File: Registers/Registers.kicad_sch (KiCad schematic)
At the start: 27 parts, among them J1 Conn_01x08_Socket, J2 Conn_01x08_Socket, J3 Conn_01x06_Pin, U1 SN74HCT245N, U2 74LS173, U3 74LS173

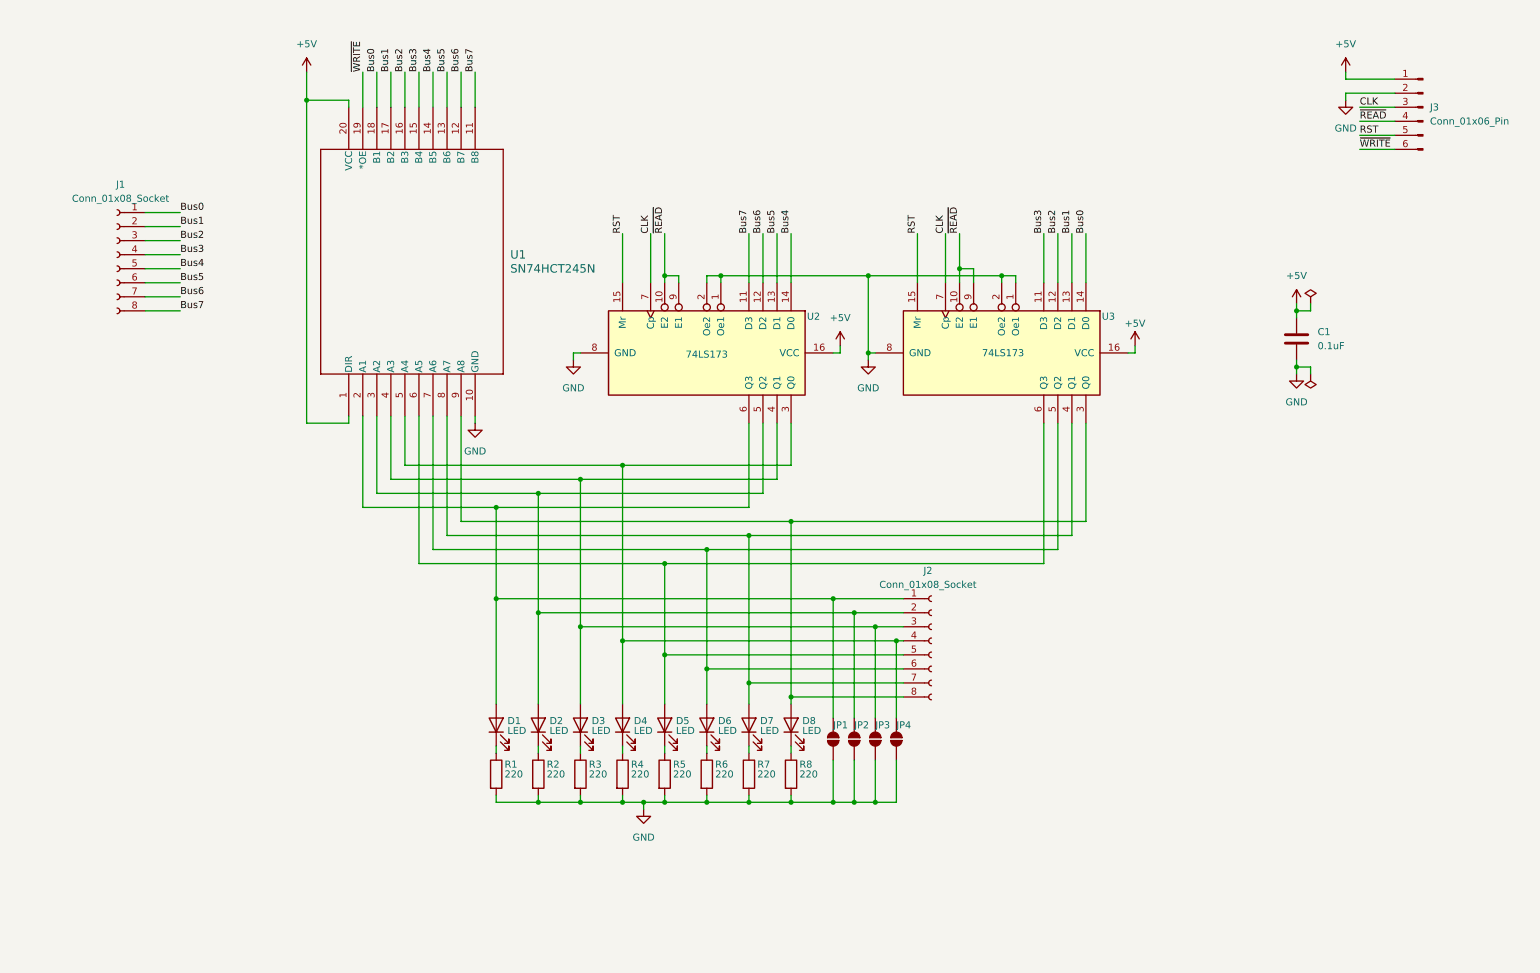
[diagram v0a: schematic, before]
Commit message: Finished routing for registers. Silkscreen and PCB shape needs to be finalized.
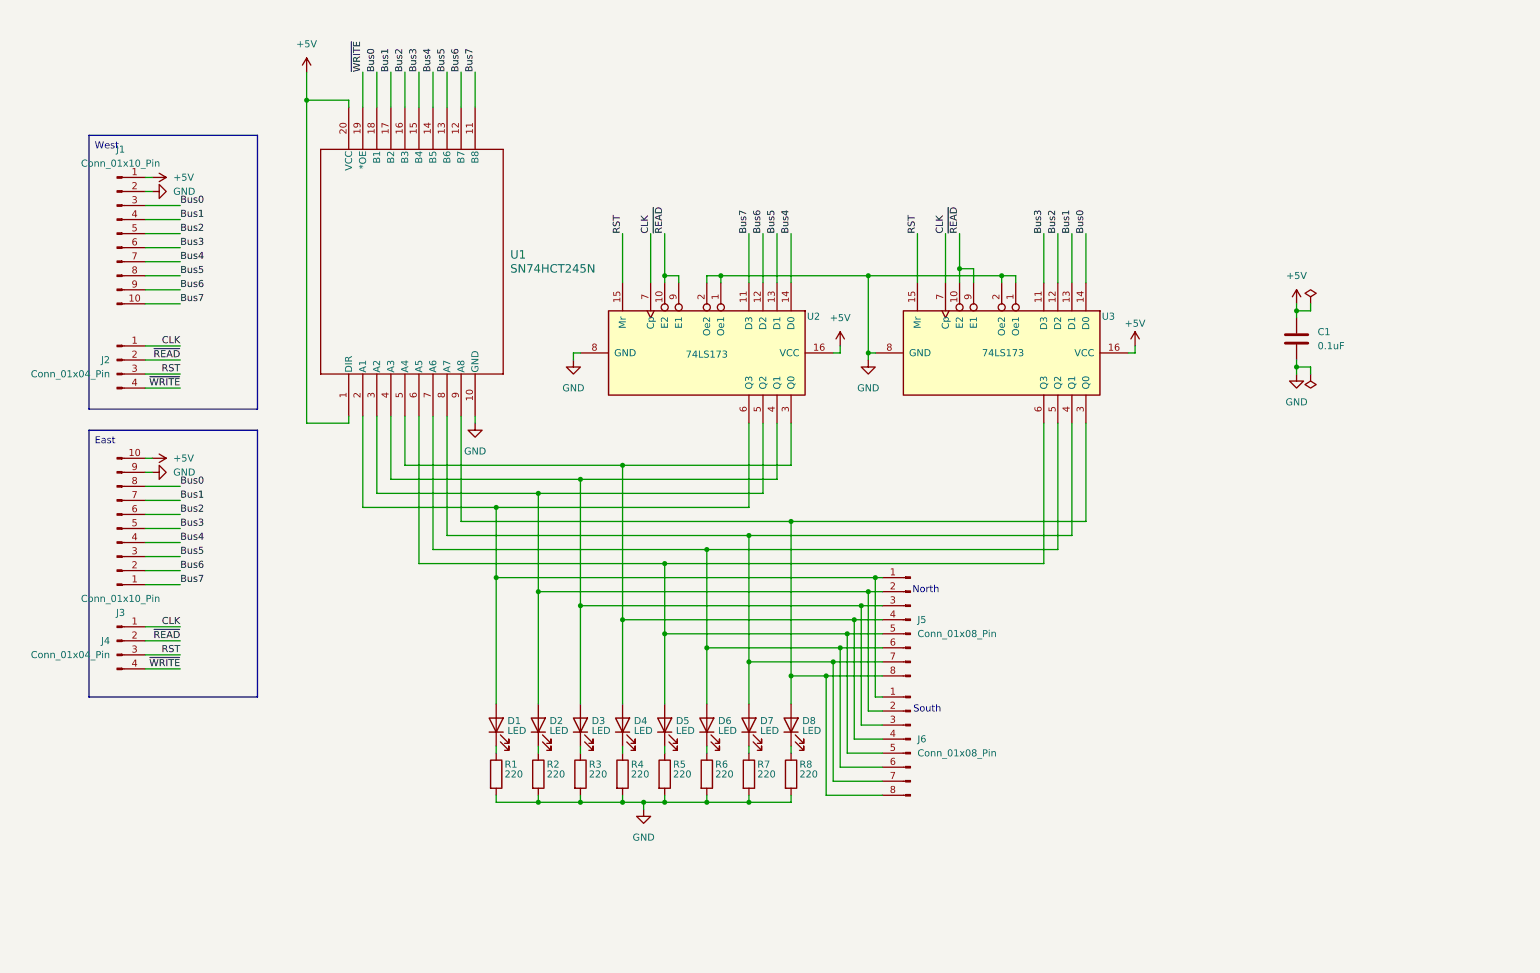
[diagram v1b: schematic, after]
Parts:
- removed J1, J2: Conn_01x08_Socket, Connector_PinHeader_1.00mm:PinHeader_1x08_P1.00mm_Horizontal, symbol Connector:Conn_01x08_Socket
- removed J3: Conn_01x06_Pin, Connector_PinHeader_1.00mm:PinHeader_1x06_P1.00mm_Horizontal, symbol Connector:Conn_01x06_Pin
- removed JP1, JP2, JP3, JP4: SolderJumper_2_Open, Jumper:SolderJumper-2_P1.3mm_Open_RoundedPad1.0x1.5mm, symbol Jumper:SolderJumper_2_Open
- added J1, J3: Conn_01x10_Pin, Connector_PinHeader_2.54mm:PinHeader_1x10_P2.54mm_Vertical, symbol Connector:Conn_01x10_Pin
- added J2, J4: Conn_01x04_Pin, Connector_PinHeader_2.54mm:PinHeader_1x04_P2.54mm_Vertical, symbol Connector:Conn_01x04_Pin
- added J5, J6: Conn_01x08_Pin, Connector_PinHeader_2.54mm:PinHeader_1x08_P2.54mm_Vertical, symbol Connector:Conn_01x08_Pin
- D1, D2, D3, D4, D5, D6, D7, D8: footprint LED_THT:LED_D2.0mm_W4.8mm_H2.5mm_FlatTop -> LED_THT:LED_D5.0mm
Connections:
- net +5V: now also J1.1 (Pin_1), J3.10 (Pin_10)
- net Bus0: now also J1.3 (Pin_3), J3.8 (Pin_8)
- net Bus1: now also J1.4 (Pin_4), J3.7 (Pin_7)
- net Bus2: now also J1.5 (Pin_5), J3.6 (Pin_6)
- net Bus3: now also J1.6 (Pin_6), J3.5 (Pin_5)
- net Bus4: now also J1.7 (Pin_7), J3.4 (Pin_4)
- net Bus5: now also J1.8 (Pin_8), J3.3 (Pin_3)
- net Bus6: now also J1.9 (Pin_9), J3.2 (Pin_2)
- net Bus7: now also J1.10 (Pin_10), J3.1 (Pin_1)
- net CLK: now also J2.1 (Pin_1), J4.1 (Pin_1)
- net GND: now also J1.2 (Pin_2), J3.9 (Pin_9)
- net RST: now also J2.3 (Pin_3), J4.3 (Pin_3)
- net ~{READ}: now also J2.2 (Pin_2), J4.2 (Pin_2)
- net ~{WRITE}: now also J2.4 (Pin_4), J4.4 (Pin_4)
- net at D8.2 (A), U1.9 (A8), U3.3 (Q0): now also J5.8 (Pin_8), J6.8 (Pin_8)
- net at D1.2 (A), U1.2 (A1), U2.6 (Q3): now also J5.1 (Pin_1), J6.1 (Pin_1)
- net at D2.2 (A), U1.3 (A2), U2.5 (Q2): now also J5.2 (Pin_2), J6.2 (Pin_2)
- net at D3.2 (A), U1.4 (A3), U2.4 (Q1): now also J5.3 (Pin_3), J6.3 (Pin_3)
- net at D4.2 (A), U1.5 (A4), U2.3 (Q0): now also J5.4 (Pin_4), J6.4 (Pin_4)
- net at D5.2 (A), U1.6 (A5), U3.6 (Q3): now also J5.5 (Pin_5), J6.5 (Pin_5)
- net at D6.2 (A), U1.7 (A6), U3.5 (Q2): now also J5.6 (Pin_6), J6.6 (Pin_6)
- net at D7.2 (A), U1.8 (A7), U3.4 (Q1): now also J5.7 (Pin_7), J6.7 (Pin_7)
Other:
- note added: "North"
- note added: "South"

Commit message: Register layout complete.
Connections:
- net Bus0: now also U2.11 (D3); no longer U3.14 (D0)
- net Bus1: now also U2.12 (D2); no longer U3.13 (D1)
- net Bus2: now also U2.13 (D1); no longer U3.12 (D2)
- net Bus3: now also U2.14 (D0); no longer U3.11 (D3)
- net Bus4: now also U3.11 (D3); no longer U2.14 (D0)
- net Bus5: now also U3.12 (D2); no longer U2.13 (D1)
- net Bus6: now also U3.13 (D1); no longer U2.12 (D2)
- net Bus7: now also U3.14 (D0); no longer U2.11 (D3)
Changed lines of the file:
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@@
 	)
 	(label "Bus7"
-		(at 142.24 62.23 90)
+		(at 203.2 62.23 90)
 		(fields_autoplaced yes)
 		(effects
@@
 	)
 	(label "Bus5"
-		(at 147.32 62.23 90)
+		(at 198.12 62.23 90)
 		(fields_autoplaced yes)
 		(effects
@@
 	)
 	(label "Bus3"
-		(at 195.58 62.23 90)
+		(at 149.86 62.23 90)
 		(fields_autoplaced yes)
 		(effects
@@
 	)
 	(label "Bus1"
-		(at 200.66 62.23 90)
+		(at 144.78 62.23 90)
 		(fields_autoplaced yes)
 		(effects
@@
 	)
 	(label "Bus4"
-		(at 149.86 62.23 90)
+		(at 195.58 62.23 90)
 		(fields_autoplaced yes)
 		(effects
@@
 	)
 	(label "Bus2"
-		(at 198.12 62.23 90)
+		(at 147.32 62.23 90)
 		(fields_autoplaced yes)
 		(effects
@@
 	)
 	(label "Bus6"
-		(at 144.78 62.23 90)
+		(at 200.66 62.23 90)
 		(fields_autoplaced yes)
 		(effects
@@
 	)
 	(label "Bus0"
-		(at 203.2 62.23 90)
-		(fields_autoplaced yes)
-		(effects
+		(at 142.24 62.23 90)
+		(fields_autoplaced yes)
+		(effects

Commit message: Added pulling resistors to unused pins from bus. (Output 2s comp & B reg write out)
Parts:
- added R9: 10k, _DownloadFootprints:CF_series_Resistors_THT, symbol Device:R
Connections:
- net +5V: now also R9.1
- net ~{WRITE}: now also R9.2
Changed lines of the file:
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@@
 		)
 	)
-	(label "Bus4"
-		(at 195.58 62.23 90)
+	(label "~{WRITE}"
+		(at 48.26 182.88 270)
 		(fields_autoplaced yes)
 		(effects
@@
 				(size 1.27 1.27)
 			)
-			(justify left bottom)
-		)
-	)
-	(label "~{READ}"
-		(at 39.37 135.89 180)
+			(justify right bottom)
+		)
+	)
+	(label "Bus4"
+		(at 195.58 62.23 90)
 		(fields_autoplaced yes)
 		(effects
@@
 				(size 1.27 1.27)
 			)
-			(justify right bottom)
-		)
-	)
-	(label "Bus4"
-		(at 39.37 118.11 0)
+			(justify left bottom)
+		)
+	)
+	(label "~{READ}"
+		(at 39.37 135.89 180)
 		(fields_autoplaced yes)
 		(effects
@@
 				(size 1.27 1.27)
 			)
-			(justify left bottom)
-		)
-	)
-	(label "Bus3"
-		(at 39.37 64.77 0)
+			(justify right bottom)
+		)
+	)
+	(label "Bus4"
+		(at 39.37 118.11 0)
 		(fields_autoplaced yes)
 		(effects
@@
 		)
 	)
-	(label "Bus2"
-		(at 39.37 62.23 0)
+	(label "Bus3"
+		(at 39.37 64.77 0)
 		(fields_autoplaced yes)
 		(effects
@@
 	)
 	(label "Bus2"
-		(at 147.32 62.23 90)
+		(at 39.37 62.23 0)
 		(fields_autoplaced yes)
 		(effects
@@
 		)
 	)
-	(label "Bus5"
-		(at 39.37 69.85 0)
+	(label "Bus2"
+		(at 147.32 62.23 90)
 		(fields_autoplaced yes)
 		(effects
@@
 		)
 	)
-	(label "Bus0"
-		(at 39.37 107.95 0)
+	(label "Bus5"
+		(at 39.37 69.85 0)
 		(fields_autoplaced yes)
 		(effects
@@
 		)
 	)
-	(label "Bus5"
-		(at 39.37 120.65 0)
+	(label "Bus0"
+		(at 39.37 107.95 0)
 		(fields_autoplaced yes)
 		(effects
@@
 		)
 	)
-	(label "~{WRITE}"
-		(at 39.37 90.17 180)
+	(label "Bus5"
+		(at 39.37 120.65 0)
 		(fields_autoplaced yes)
 		(effects
@@
 				(size 1.27 1.27)
 			)
-			(justify right bottom)
-		)
-	)
-	(label "Bus1"
-		(at 77.47 33.02 90)
+			(justify left bottom)
+		)
+	)
+	(label "~{WRITE}"
+		(at 39.37 90.17 180)
 		(fields_autoplaced yes)
 		(effects
@@
 				(size 1.27 1.27)
 			)
-			(justify left bottom)
-		)
-	)
-	(label "CLK"
-		(at 124.46 62.23 90)
+			(justify right bottom)
+		)
+	)
+	(label "Bus1"
+		(at 77.47 33.02 90)
 		(fields_autoplaced yes)
 		(effects
@@
 	)
 	(label "CLK"
-		(at 177.8 62.23 90)
+		(at 124.46 62.23 90)
 		(fields_autoplaced yes)
 		(effects
@@
 		)
 	)
-	(label "Bus6"
-		(at 90.17 33.02 90)
+	(label "CLK"
+		(at 177.8 62.23 90)
 		(fields_autoplaced yes)
 		(effects
@@
 		)
 	)
-	(label "CLK"
-		(at 39.37 82.55 180)
+	(label "Bus6"
+		(at 90.17 33.02 90)
 		(fields_autoplaced yes)
 		(effects
@@
 				(size 1.27 1.27)
 			)
-			(justify right bottom)
-		)
-	)
-	(label "~{WRITE}"
-		(at 39.37 140.97 180)
+			(justify left bottom)
+		)
+	)
+	(label "CLK"
+		(at 39.37 82.55 180)
 		(fields_autoplaced yes)
 		(effects
@@
 		)
 	)
-	(label "Bus6"
-		(at 200.66 62.23 90)
+	(label "~{WRITE}"
+		(at 39.37 140.97 180)
 		(fields_autoplaced yes)
 		(effects
@@
 				(size 1.27 1.27)
 			)
-			(justify left bottom)
-		)
-	)
-	(label "Bus0"
-		(at 74.93 33.02 90)
+			(justify right bottom)
+		)
+	)
+	(label "Bus6"
+		(at 200.66 62.23 90)
 		(fields_autoplaced yes)
 		(effects
@@
 		)
 	)
-	(label "~{READ}"
-		(at 180.34 62.23 90)
+	(label "Bus0"
+		(at 74.93 33.02 90)
 		(fields_autoplaced yes)
 		(effects
@@
 		)
 	)
-	(label "Bus2"
-		(at 39.37 113.03 0)
+	(label "~{READ}"
+		(at 180.34 62.23 90)
 		(fields_autoplaced yes)
 		(effects
@@
 		)
 	)
-	(label "~{READ}"
-		(at 127 62.23 90)
+	(label "Bus2"
+		(at 39.37 113.03 0)
 		(fields_autoplaced yes)
 		(effects
@@
 		)
 	)
-	(label "~{WRITE}"
-		(at 72.39 33.02 90)
+	(label "~{READ}"
+		(at 127 62.23 90)
 		(fields_autoplaced yes)
 		(effects
@@
 		)
 	)
-	(label "Bus0"
-		(at 142.24 62.23 90)
+	(label "~{WRITE}"
+		(at 72.39 33.02 90)
 		(fields_autoplaced yes)
 		(effects
@@
 		)
 	)
-	(label "RST"
-		(at 172.72 62.23 90)
+	(label "Bus0"
+		(at 142.24 62.23 90)
 		(fields_autoplaced yes)
 		(effects
@@
 	)
 	(label "RST"
-		(at 39.37 138.43 180)
+		(at 172.72 62.23 90)
 		(fields_autoplaced yes)
 		(effects
@@
 				(size 1.27 1.27)
 			)
-			(justify right bottom)
+			(justify left bottom)
 		)
 	)
 	(label "RST"
-		(at 119.38 62.23 90)
+		(at 39.37 138.43 180)
 		(fields_autoplaced yes)
 		(effects
@@
 				(size 1.27 1.27)
 			)
-			(justify left bottom)
-		)
-	)
-	(label "Bus7"
-		(at 92.71 33.02 90)
+			(justify right bottom)
+		)
+	)
+	(label "RST"
+		(at 119.38 62.23 90)
 		(fields_autoplaced yes)
 		(effects
@@
 		)
 	)
+	(label "Bus7"
+		(at 92.71 33.02 90)
+		(fields_autoplaced yes)
+		(effects
+			(font
+				(size 1.27 1.27)
+			)
+			(justify left bottom)
+		)
+	)
 	(symbol
 		(lib_id "Device:LED")
@@
 	)
 	(symbol
+		(lib_id "power:+5V")
+		(at 48.26 175.26 0)
+		(unit 1)
+		(exclude_from_sim no)
+		(in_bom yes)
+		(on_board yes)
+		(dnp no)
+		(fields_autoplaced yes)
+		(property "Reference" "#PWR014"
+			(at 48.26 179.07 0)
+			(effects
+				(font
+					(size 1.27 1.27)
+				)
+				(hide yes)
+			)
+		)
+		(property "Value" "+5V"
+			(at 48.26 170.18 0)
+			(effects
+				(font
+					(size 1.27 1.27)
+				)
+			)
+		)
+		(property "Footprint" ""
+			(at 48.26 175.26 0)
+			(effects
+				(font
+					(size 1.27 1.27)
+				)
+				(hide yes)
+			)
+		)
+		(property "Datasheet" ""
+			(at 48.26 175.26 0)
+			(effects
+				(font
+					(size 1.27 1.27)
+				)
+				(hide yes)
+			)
+		)
+		(property "Description" "Power symbol creates a global label with name \"+5V\""
+			(at 48.26 175.26 0)
+			(effects
+				(font
+					(size 1.27 1.27)
+				)
+				(hide yes)
+			)
+		)
+		(pin "1"
+		)
+		(instances
+			(project ""
+				(path "/6db53e48-b6be-4498-bb6c-c508b16e3b63"
+					(reference "#PWR014")
+					(unit 1)
+				)
+			)
+		)
+	)
+	(symbol
 		(lib_id "Device:LED")
 		(at 96.52 151.13 90)
@@
 					(unit 1)
 				)
+			)
+		)
+	)
+	(symbol
+		(lib_id "Device:R")
+		(at 48.26 179.07 0)
+		(unit 1)
+		(exclude_from_sim no)
+		(in_bom yes)
+		(on_board yes)
+		(dnp no)
+		(property "Reference" "R9"
+			(at 49.784 177.292 0)
+			(effects
+				(font
+					(size 1.27 1.27)
+				)
+				(justify left)
+			)
+		)
+		(property "Value" "10k"
+			(at 49.784 179.07 0)
+			(effects
+				(font
+					(size 1.27 1.27)
+				)
+				(justify left)
+			)
+		)
+		(property "Footprint" "_DownloadFootprints:CF_series_Resistors_THT"
+			(at 46.482 179.07 90)
+			(effects
+				(font
+					(size 1.27 1.27)
+				)
+				(hide yes)
+			)
+		)
+		(property "Datasheet" "~"
+			(at 48.26 179.07 0)
+			(effects
+				(font
+					(size 1.27 1.27)
+				)
+				(hide yes)
+			)
+		)
+		(property "Description" "Resistor"
+			(at 48.26 179.07 0)
+			(effects
+				(font
+					(size 1.27 1.27)
+				)
+				(hide yes)
+			)
+		)
+		(pin "2"
+		)
+		(pin "1"
+		)
+		(instances
+			(project "Registers"
+				(path "/6db53e48-b6be-4498-bb6c-c508b16e3b63"
+					(reference "R9")
+					(unit 1)
+				)
